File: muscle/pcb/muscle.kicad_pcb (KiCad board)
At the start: 4 copper layers, 119.5 x 50 mm, 143 parts, among them J1 B4B-XH-2(LF)(SN), J10 USB4115-03-C, J2 WAFER-SH1.0-3PWB, J3 XT30UPB-M, J4 WAFER-SH1.0-3PWB, J5 B4B-XH-2(LF)(SN), J8 B2B-XH-A(LF)(SN), Q2 WSD4070DN33, Q3 WSD4070DN33, Q4 WSD4070DN33, Q5 BSS138W, Q6 WSD4070DN33, Q8 WSD4070DN33, SW1 GT-TC041B-H036-L1N, SW2 GT-TC041B-H036-L1N, U1 TMC2209-LA, U12 TPD2EUSB30A, U13 TLV75733PDBV, U14 DRV8701P, U17 TPS16630PWP, U2 TMC2209-LA, U3 RP2350A, U4 LM5050-1, U5 TPS2061CDBV, U6 XT25F128FWOIGT-W, U7 LM393BIDSGR, U8 TUSB320LI, U9 TPS62933, Y1 ABM8-272-T3

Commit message: muscle: tweaks
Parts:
- moved TP7 7.51 mm to (105.5, 105.2)
- moved JP15 1.90 mm to (102.5, 105.2)
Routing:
- net +3V3: track 137.9 -> 147.0 mm
- net Net-(U17-IMON): track 6.43 -> 14.1 mm
- net /~{DRV_EN}: track 112.9 -> 116.8 mm
- net /PGOOD: track 44.7 -> 41.7 mm
- net Net-(U4-IN): track 14.3 -> 12.6 mm
- net Net-(Q2-G): track 8.17 -> 6.55 mm
- net GND: track 125.7 -> 127.0 mm, vias 150 -> 157
- net Net-(J3-N): track 7.97 -> 7.33 mm

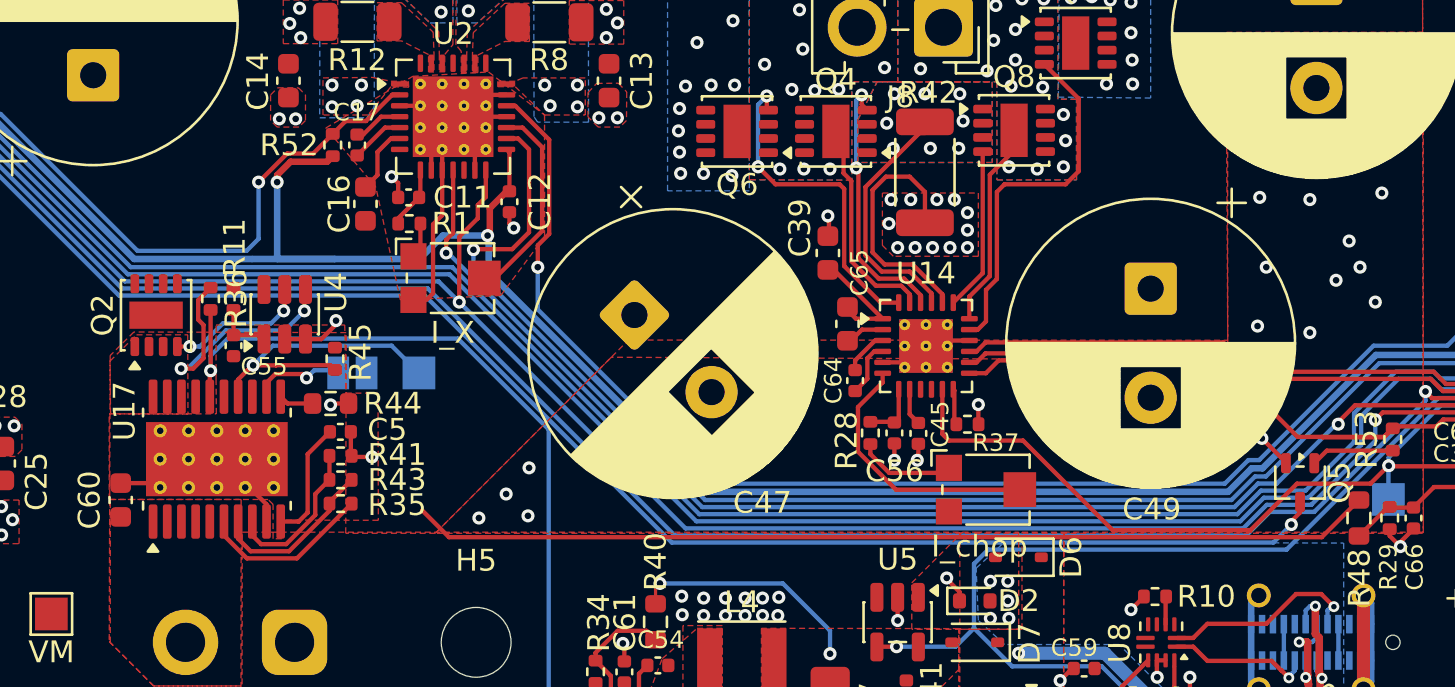
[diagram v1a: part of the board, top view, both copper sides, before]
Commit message: muscle: make I_LIM adjustable
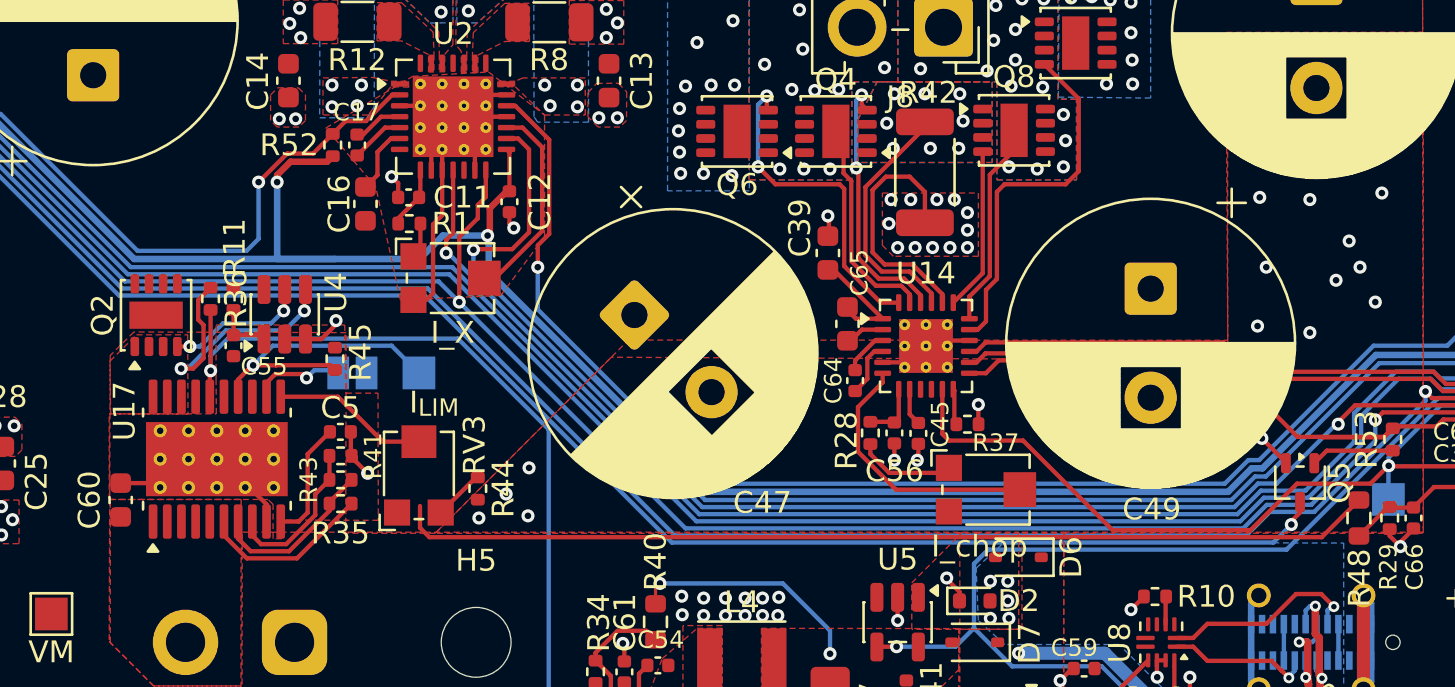
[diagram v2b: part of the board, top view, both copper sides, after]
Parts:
- added RV3: I_{LIM}, Potentiometer_SMD:Potentiometer_Bourns_TC33X_Vertical, F.Cu at (105.5, 109.8)
- R44: value 3.9k -> 3k; footprint Resistor_SMD:R_0603_1608Metric -> Resistor_SMD:R_0402_1005Metric
- moved R44 7.80 mm to (108.2, 110.5), turned to -90 degrees
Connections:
- R44 pad 1: Net-(U17-ILIM) -> Net-(R44-Pad1)
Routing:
- net Net-(U17-ILIM): track 1.59 -> 7.19 mm
- net Net-(R44-Pad1): track 0.00 -> 2.28 mm
- net GND: track 127.0 -> 126.4 mm, vias 157 -> 156

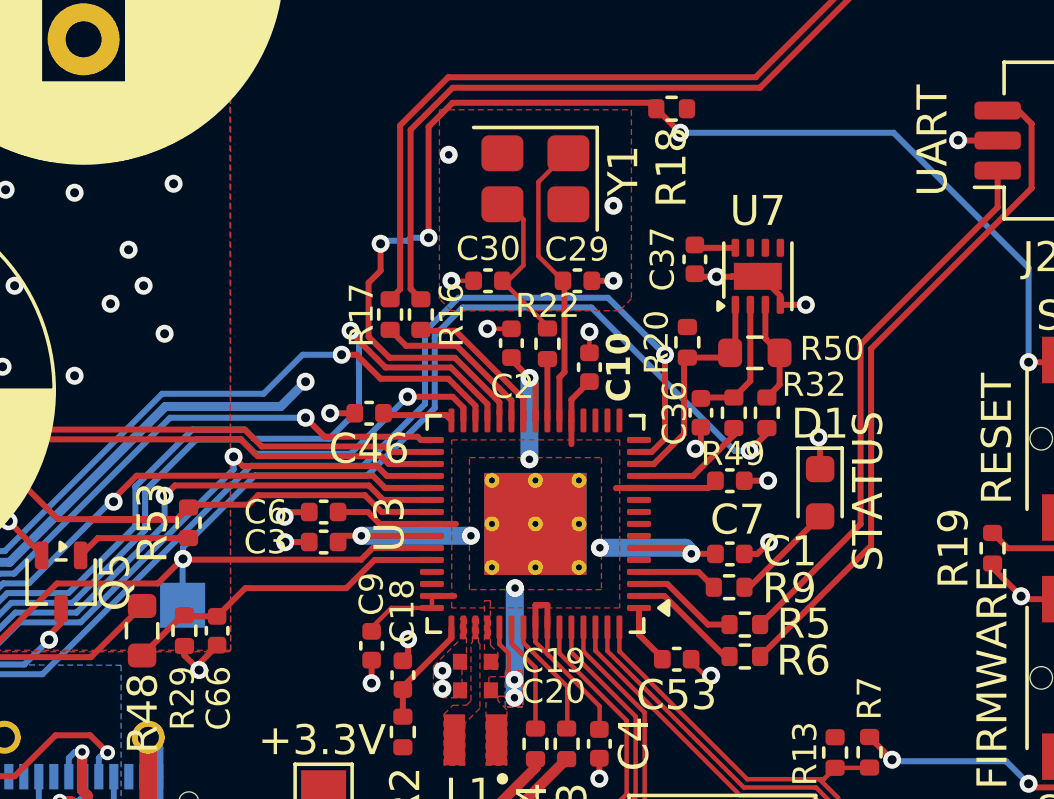
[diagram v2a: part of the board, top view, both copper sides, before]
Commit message: muscle: throw away analog comparator
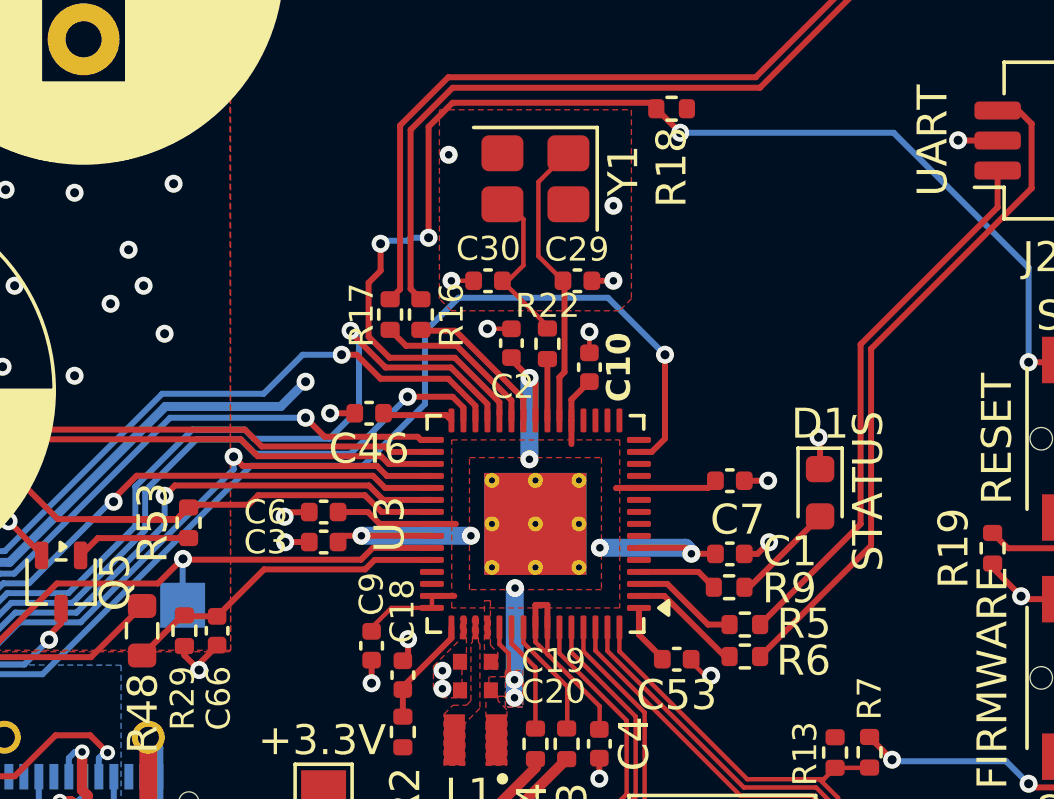
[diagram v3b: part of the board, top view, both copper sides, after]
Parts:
- removed C36, C37: 1u, Capacitor_SMD:C_0402_1005Metric
- removed R20: 10k, Resistor_SMD:R_0402_1005Metric
- removed R32: 1k, Resistor_SMD:R_0402_1005Metric
- removed R49: 5.1k, Resistor_SMD:R_0402_1005Metric
- removed R50: 150k, Resistor_SMD:R_0603_1608Metric
- removed U7: LM393BIDSGR, Package_SON:Texas_DSG0008A_WSON-8-1EP_2x2mm_P0.5mm_EP0.9x1.6mm
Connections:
- U3 pad 12: /S_SENSE_PWM -> unconnected-(U3-GPIO8-Pad12)
- U3 pad 13: /S_SENSE_COMP -> unconnected-(U3-GPIO9-Pad13)
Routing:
- net /S_SENSE: track 62.6 -> 35.6 mm, vias 2 -> 1
- net /S_SENSE_COMP: track 7.04 -> 0.00 mm
- net GND: track 126.4 -> 121.5 mm, vias 156 -> 153
- net Net-(U7A--): track 4.39 -> 0.00 mm
- net /S_SENSE_PWM: track 3.96 -> 0.00 mm
- net Net-(U7A-+): track 3.46 -> 0.00 mm
- net +3V3: track 147.0 -> 145.7 mm

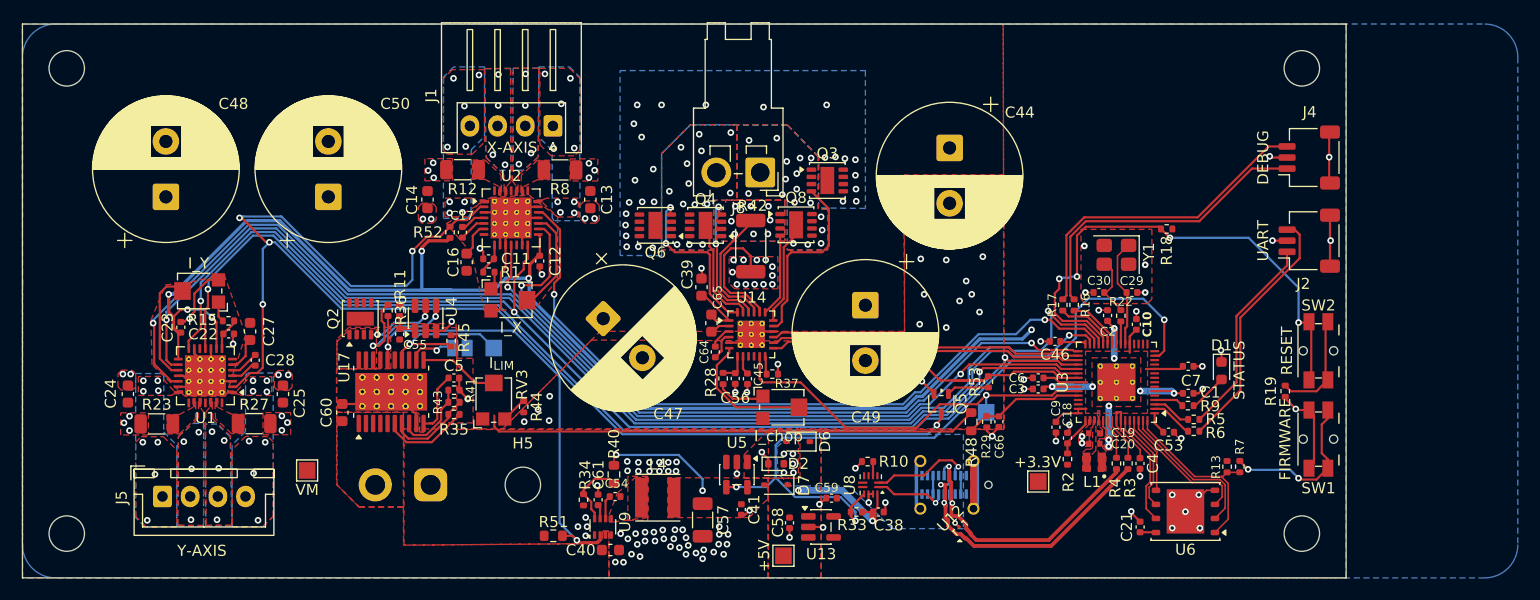
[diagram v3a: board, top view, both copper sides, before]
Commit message: muscle: use PGOOD for voltage monitoring
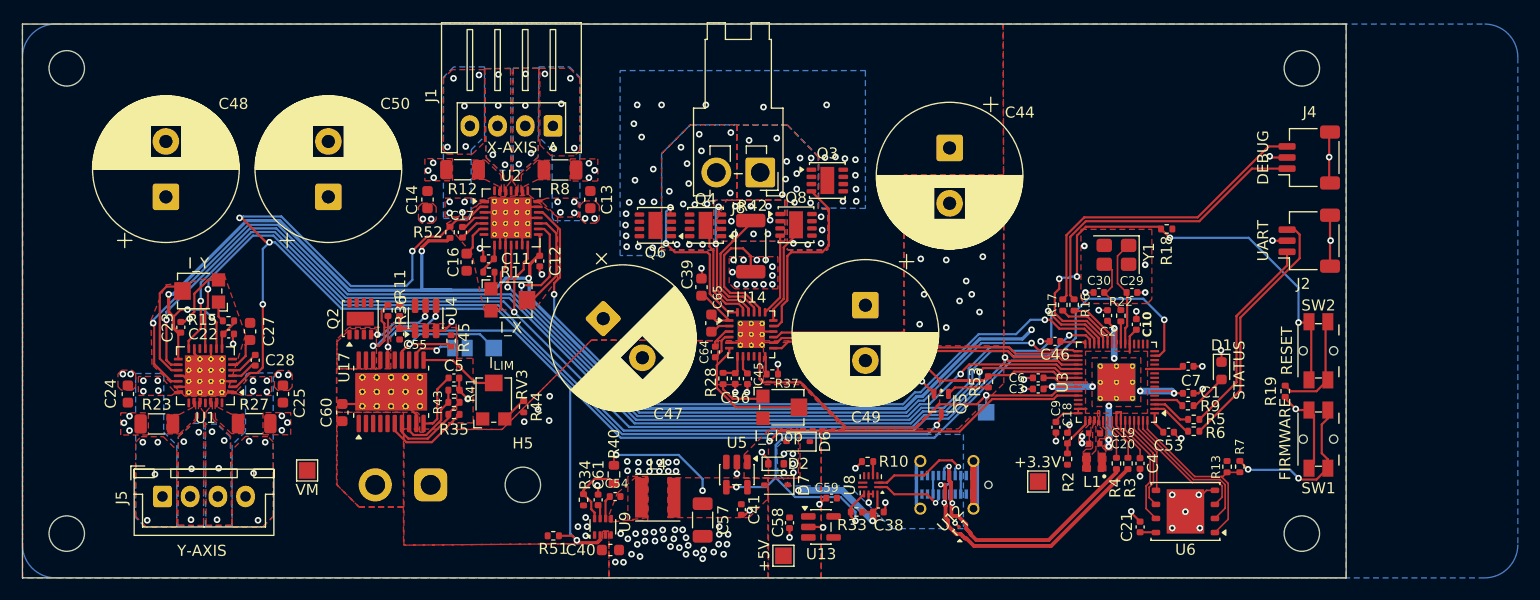
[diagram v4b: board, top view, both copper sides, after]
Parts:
- removed C66: 100p, Capacitor_SMD:C_0402_1005Metric
- removed R29: 10k, Resistor_SMD:R_0402_1005Metric
- removed R48: 68k, Resistor_SMD:R_0603_1608Metric
- R51: value 68k -> 33k; footprint Resistor_SMD:R_0603_1608Metric -> Resistor_SMD:R_0402_1005Metric
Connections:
- U3 pad 41: /VM_SENSE -> /PGOOD
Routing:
- net /PGOOD: track 41.7 -> 91.3 mm, vias 2 -> 3
- net VM: track 49.9 -> 4.94 mm
- net /VM_SENSE: track 10.9 -> 0.00 mm
- net GND: track 121.5 -> 119.5 mm, vias 153 -> 152

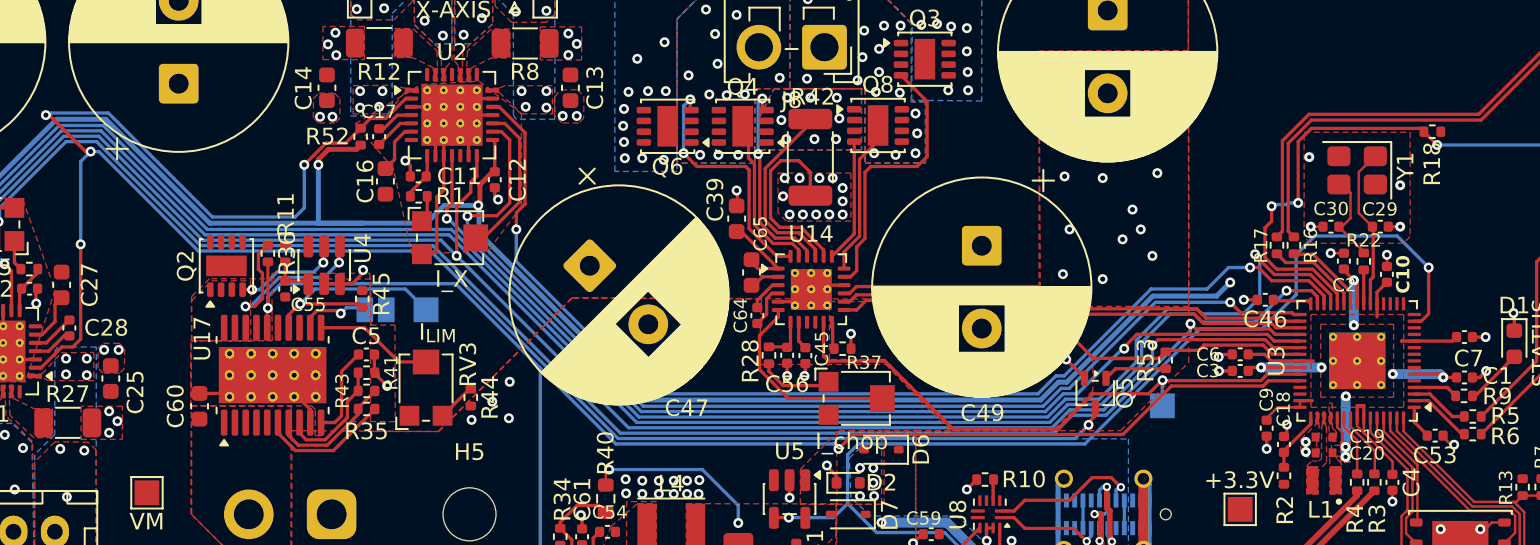
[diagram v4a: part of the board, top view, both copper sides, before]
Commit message: muscle: free up GPIOs reserved on the pico2
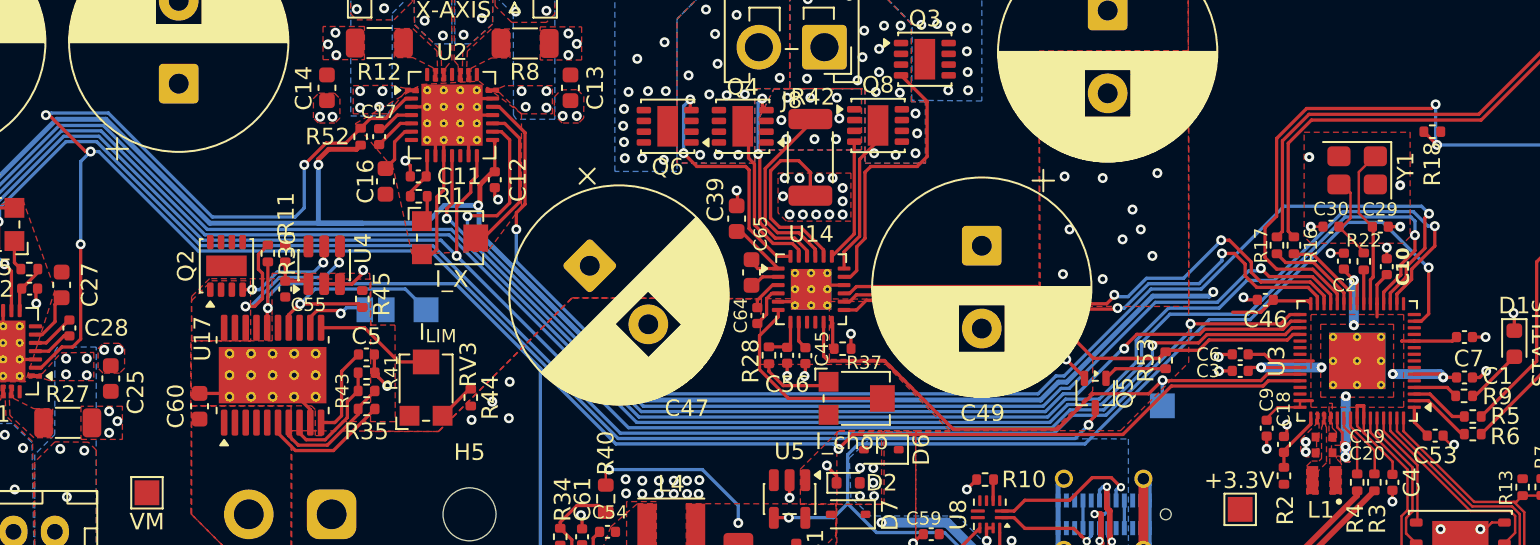
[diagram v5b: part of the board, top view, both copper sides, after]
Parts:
- moved C10 0.46 mm to (163.6, 102.7)
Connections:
- U3 pad 17: unconnected-(U3-GPIO13-Pad17) -> /Y_DIR
- U3 pad 18: unconnected-(U3-GPIO14-Pad18) -> /X_DIR
- U3 pad 19: unconnected-(U3-GPIO15-Pad19) -> /Y_STEP
- U3 pad 27: /Y_DIR -> /X_STEP
- U3 pad 28: /X_DIR -> /S_IN1
- U3 pad 29: /Y_STEP -> /S_IN2
- U3 pad 31: /X_STEP -> /Y_DIAG
- U3 pad 32: /S_IN1 -> /X_DIAG
- U3 pad 33: /S_IN2 -> /STEP_UART
- U3 pad 34: /Y_DIAG -> /DRV_EN
- U3 pad 35: /X_DIAG -> unconnected-(U3-GPIO23-Pad35)
- U3 pad 36: /STEP_UART -> unconnected-(U3-GPIO24-Pad36)
- U3 pad 37: /DRV_EN -> unconnected-(U3-GPIO25-Pad37)
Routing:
- net /X_DIR: track 67.0 -> 80.3 mm
- net /Y_STEP: track 104.4 -> 117.0 mm
- net /Y_DIR: track 111.6 -> 121.2 mm
- net /S_IN1: track 28.6 -> 33.6 mm, vias 0 -> 2
- net /S_IN2: track 28.5 -> 32.7 mm, vias 0 -> 2
- net /RESET: track 45.8 -> 49.6 mm, vias 4 -> 3
- net /X_STEP: track 66.3 -> 69.9 mm
- net +3V3: track 145.7 -> 147.7 mm
- net /USB_ROLE: track 66.7 -> 66.0 mm
